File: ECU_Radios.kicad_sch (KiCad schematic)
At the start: 8 parts, among them J19 SMA, J20 SMA

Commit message: addressed PR comments
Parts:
- added C94, C96: 10uF, Capacitor_SMD:C_0603_1608Metric, symbol Device:C_Small
- added J21, J23: SMA, Connector_Coaxial:SMA_Molex_73251-2200_Horizontal, symbol Connector:Conn_Coaxial
- added R117, R119: 100k, Resistor_SMD:R_0603_1608Metric_Pad0.98x0.95mm_HandSolder, symbol Device:R_Small_US
- added U44, U46: ~, UCIRP-KiCAD-Lib:RFM95W, symbol UCIRP-KiCAD-Lib:RFM95W
- renumbered C92 to C93, C93 to C95, J19 to J20, J20 to J22, R113 to R116, R114 to R118, U42 to U43, U43 to U45
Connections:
- net +3.3V: now also C94.1, C96.1, R117.1, R119.1, U44.13 (3.3V), U46.13 (3.3V)
- net GND: now also C94.2, C96.2, J21.2 (Ext), J23.2 (Ext), U44.1 (GND), U44.10 (GND), U44.8 (GND), U46.1 (GND), U46.10 (GND), U46.8 (GND)
- net RADIO_MISO: now also U44.2 (MISO), U46.2 (MISO)
- net RADIO_MOSI: now also U44.3 (MOSI), U46.3 (MOSI)
- net RADIO_SCK: now also U44.4 (SCK), U46.4 (SCK)
- new net: R117.2, U44.5 (~{CS})
- new net: J21.1 (In), U44.9 (ANT)
- new net: R119.2, U46.5 (~{CS})
- new net: J23.1 (In), U46.9 (ANT)
- no-connect marks 8 -> 16
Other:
- note added: "NEED TO ADD DIO, RST, and CS PINS"
- note added: "TRS Radio Module 3"
- note added: "TRS Radio Module 4"
- moved on the sheet: C93, C95, J20, J22, R116, R118, U43, U45

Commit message: Updated schematic with IOC
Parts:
- removed C96: 10uF, Capacitor_SMD:C_0603_1608Metric, symbol Device:C_Small
- removed J23: SMA, Connector_Coaxial:SMA_Molex_73251-2200_Horizontal, symbol Connector:Conn_Coaxial
- removed R119: 100k, Resistor_SMD:R_0603_1608Metric_Pad0.98x0.95mm_HandSolder, symbol Device:R_Small_US
- removed U46: ~, UCIRP-KiCAD-Lib:RFM95W, symbol UCIRP-KiCAD-Lib:RFM95W
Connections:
- net RADIO2_DIO0: now reaches U44.14 (DIO0)
- net RADIO2_DIO1: now reaches U44.15 (DIO1)
- net RADIO2_nCS: now reaches R117.2, U44.5 (~{CS})
- net RADIO2_nRST: now reaches U44.6 (~{RST})
- no-connect marks 16 -> 12
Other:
- note removed: "NEED TO ADD DIO, RST, and CS PINS"
- note removed: "TRS Radio Module 4"
- moved on the sheet: C94, J21, R117, U44

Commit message: Assigned almost all footprints
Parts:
- R116, R117, R118: value 100k -> 100K; footprint Resistor_SMD:R_0603_1608Metric_Pad0.98x0.95mm_HandSolder -> Resistor_SMD:R_0402_1005Metric; Part # Generic 100k 1% 0402 Chip Resistor -> Generic 100K 5% 0402 Resistor
- U43, U44, U45: footprint UCIRP-KiCAD-Lib:RFM95W -> 0UCIRP-KiCAD-Lib:RFM95W
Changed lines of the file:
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@@
 			)
 		)
-		(property "Footprint" "UCIRP-KiCAD-Lib:RFM95W"
+		(property "Footprint" "0UCIRP-KiCAD-Lib:RFM95W"
 			(at 137.16 129.54 0)
 			(effects
@@
 		(on_board yes)
 		(dnp no)
-		(property "Reference" "#PWR0299"
+		(property "Reference" "#PWR0301"
 			(at 172.72 125.73 0)
 			(effects
@@
 			(project "rocket2-ecu"
 				(path "/02606b2c-b376-4ffb-9781-f9cea3f70994/2e42eb37-4c52-4f5f-835d-7e84f50db3a9"
-					(reference "#PWR0299")
+					(reference "#PWR0301")
 					(unit 1)
 				)
@@
 		(on_board yes)
 		(dnp no)
-		(property "Reference" "#PWR0304"
+		(property "Reference" "#PWR0302"
 			(at 191.77 57.15 0)
 			(effects
@@
 			(project "rocket2-ecu"
 				(path "/02606b2c-b376-4ffb-9781-f9cea3f70994/2e42eb37-4c52-4f5f-835d-7e84f50db3a9"
-					(reference "#PWR0304")
+					(reference "#PWR0302")
 					(unit 1)
 				)
@@
 		(on_board yes)
 		(dnp no)
-		(property "Reference" "#PWR0300"
+		(property "Reference" "#PWR0298"
 			(at 158.75 88.9 0)
 			(effects
@@
 			(project "rocket2-ecu"
 				(path "/02606b2c-b376-4ffb-9781-f9cea3f70994/2e42eb37-4c52-4f5f-835d-7e84f50db3a9"
-					(reference "#PWR0300")
+					(reference "#PWR0298")
 					(unit 1)
 				)
@@
 		(on_board yes)
 		(dnp no)
-		(property "Reference" "#PWR0309"
+		(property "Reference" "#PWR0305"
 			(at 227.33 66.04 0)
 			(effects
@@
 			(project "rocket2-ecu"
 				(path "/02606b2c-b376-4ffb-9781-f9cea3f70994/2e42eb37-4c52-4f5f-835d-7e84f50db3a9"
-					(reference "#PWR0309")
+					(reference "#PWR0305")
 					(unit 1)
 				)
@@
 		(on_board yes)
 		(dnp no)
-		(property "Reference" "#PWR0289"
+		(property "Reference" "#PWR0292"
 			(at 104.14 148.59 0)
 			(effects
@@
 			(project "rocket2-ecu"
 				(path "/02606b2c-b376-4ffb-9781-f9cea3f70994/2e42eb37-4c52-4f5f-835d-7e84f50db3a9"
-					(reference "#PWR0289")
+					(reference "#PWR0292")
 					(unit 1)
 				)
@@
 		(on_board yes)
 		(dnp no)
-		(property "Reference" "#PWR0290"
+		(property "Reference" "#PWR0289"
 			(at 59.69 58.42 0)
 			(effects
@@
 			(project "rocket2-ecu"
 				(path "/02606b2c-b376-4ffb-9781-f9cea3f70994/2e42eb37-4c52-4f5f-835d-7e84f50db3a9"
-					(reference "#PWR0290")
+					(reference "#PWR0289")
 					(unit 1)
 				)
@@
 		(on_board yes)
 		(dnp no)
-		(property "Reference" "#PWR0292"
+		(property "Reference" "#PWR0290"
 			(at 91.44 57.15 0)
 			(effects
@@
 			(project "rocket2-ecu"
 				(path "/02606b2c-b376-4ffb-9781-f9cea3f70994/2e42eb37-4c52-4f5f-835d-7e84f50db3a9"
-					(reference "#PWR0292")
+					(reference "#PWR0290")
 					(unit 1)
 				)
@@
 			)
 		)
-		(property "Footprint" "UCIRP-KiCAD-Lib:RFM95W"
+		(property "Footprint" "0UCIRP-KiCAD-Lib:RFM95W"
 			(at 91.44 69.85 0)
 			(effects
@@
 			)
 		)
-		(property "Value" "100k"
+		(property "Value" "100K"
 			(at 62.23 58.42 0)
 			(effects
@@
 			)
 		)
-		(property "Footprint" "Resistor_SMD:R_0603_1608Metric_Pad0.98x0.95mm_HandSolder"
+		(property "Footprint" "Resistor_SMD:R_0402_1005Metric"
 			(at 59.69 57.15 0)
 			(effects
@@
 			)
 		)
-		(property "Part #" "Generic 100k 1% 0402 Chip Resistor"
+		(property "Part #" "Generic 100K 5% 0402 Resistor"
 			(at 59.69 57.15 0)
 			(effects
@@
 		(on_board yes)
 		(dnp no)
-		(property "Reference" "#PWR0302"
+		(property "Reference" "#PWR0299"
 			(at 160.02 58.42 0)
 			(effects
@@
 			(project "rocket2-ecu"
 				(path "/02606b2c-b376-4ffb-9781-f9cea3f70994/2e42eb37-4c52-4f5f-835d-7e84f50db3a9"
-					(reference "#PWR0302")
+					(reference "#PWR0299")
 					(unit 1)
 				)
@@
 		(on_board yes)
 		(dnp no)
-		(property "Reference" "#PWR0296"
+		(property "Reference" "#PWR0294"
 			(at 127 58.42 0)
 			(effects
@@
 			(project "rocket2-ecu"
 				(path "/02606b2c-b376-4ffb-9781-f9cea3f70994/2e42eb37-4c52-4f5f-835d-7e84f50db3a9"
-					(reference "#PWR0296")
+					(reference "#PWR0294")
 					(unit 1)
 				)
@@
 		(on_board yes)
 		(dnp no)
-		(property "Reference" "#PWR0305"
+		(property "Reference" "#PWR0303"
 			(at 191.77 95.25 0)
 			(effects
@@
 			(project "rocket2-ecu"
 				(path "/02606b2c-b376-4ffb-9781-f9cea3f70994/2e42eb37-4c52-4f5f-835d-7e84f50db3a9"
-					(reference "#PWR0305")
+					(reference "#PWR0303")
 					(unit 1)
 				)
@@
 		(on_board yes)
 		(dnp no)
-		(property "Reference" "#PWR0297"
+		(property "Reference" "#PWR0295"
 			(at 127 66.04 0)
 			(effects
@@
 			(project "rocket2-ecu"
 				(path "/02606b2c-b376-4ffb-9781-f9cea3f70994/2e42eb37-4c52-4f5f-835d-7e84f50db3a9"
-					(reference "#PWR0297")
+					(reference "#PWR0295")
 					(unit 1)
 				)
@@
 		(on_board yes)
 		(dnp no)
-		(property "Reference" "#PWR0298"
+		(property "Reference" "#PWR0300"
 			(at 172.72 118.11 0)
 			(effects
@@
 			(project "rocket2-ecu"
 				(path "/02606b2c-b376-4ffb-9781-f9cea3f70994/2e42eb37-4c52-4f5f-835d-7e84f50db3a9"
-					(reference "#PWR0298")
+					(reference "#PWR0300")
 					(unit 1)
 				)
@@
 		(on_board yes)
 		(dnp no)
-		(property "Reference" "#PWR0291"
+		(property "Reference" "#PWR0293"
 			(at 105.41 118.11 0)
 			(effects
@@
 			(project "rocket2-ecu"
 				(path "/02606b2c-b376-4ffb-9781-f9cea3f70994/2e42eb37-4c52-4f5f-835d-7e84f50db3a9"
-					(reference "#PWR0291")
+					(reference "#PWR0293")
 					(unit 1)
 				)
@@
 			)
 		)
-		(property "Value" "100k"
+		(property "Value" "100K"
 			(at 162.56 58.42 0)
 			(effects
@@
 			)
 		)
-		(property "Footprint" "Resistor_SMD:R_0603_1608Metric_Pad0.98x0.95mm_HandSolder"
+		(property "Footprint" "Resistor_SMD:R_0402_1005Metric"
 			(at 160.02 57.15 0)
 			(effects
@@
 			)
 		)
-		(property "Part #" "Generic 100k 1% 0402 Chip Resistor"
+		(property "Part #" "Generic 100K 5% 0402 Resistor"
 			(at 160.02 57.15 0)
 			(effects
@@
 		(on_board yes)
 		(dnp no)
-		(property "Reference" "#PWR0295"
+		(property "Reference" "#PWR0297"
 			(at 137.16 154.94 0)
 			(effects
@@
 			(project "rocket2-ecu"
 				(path "/02606b2c-b376-4ffb-9781-f9cea3f70994/2e42eb37-4c52-4f5f-835d-7e84f50db3a9"
-					(reference "#PWR0295")
+					(reference "#PWR0297")
 					(unit 1)
 				)
@@
 			)
 		)
-		(property "Footprint" "UCIRP-KiCAD-Lib:RFM95W"
+		(property "Footprint" "0UCIRP-KiCAD-Lib:RFM95W"
 			(at 191.77 69.85 0)
 			(effects
@@
 		(on_board yes)
 		(dnp no)
-		(property "Reference" "#PWR0293"
+		(property "Reference" "#PWR0291"
 			(at 91.44 95.25 0)
 			(effects
@@
 			(project "rocket2-ecu"
 				(path "/02606b2c-b376-4ffb-9781-f9cea3f70994/2e42eb37-4c52-4f5f-835d-7e84f50db3a9"
-					(reference "#PWR0293")
+					(reference "#PWR0291")
 					(unit 1)
 				)
@@
 			)
 		)
-		(property "Value" "100k"
+		(property "Value" "100K"
 			(at 107.95 118.11 0)
 			(effects
@@
 			)
 		)
-		(property "Footprint" "Resistor_SMD:R_0603_1608Metric_Pad0.98x0.95mm_HandSolder"
+		(property "Footprint" "Resistor_SMD:R_0402_1005Metric"
 			(at 105.41 116.84 0)
 			(effects
@@
 			)
 		)
-		(property "Part #" "Generic 100k 1% 0402 Chip Resistor"
+		(property "Part #" "Generic 100K 5% 0402 Resistor"
 			(at 105.41 116.84 0)
 			(effects
@@
 		(on_board yes)
 		(dnp no)
-		(property "Reference" "#PWR0294"
+		(property "Reference" "#PWR0296"
 			(at 137.16 116.84 0)
 			(effects
@@
 			(project "rocket2-ecu"
 				(path "/02606b2c-b376-4ffb-9781-f9cea3f70994/2e42eb37-4c52-4f5f-835d-7e84f50db3a9"
-					(reference "#PWR0294")
+					(reference "#PWR0296")
 					(unit 1)
 				)
@@
 		(on_board yes)
 		(dnp no)
-		(property "Reference" "#PWR0308"
+		(property "Reference" "#PWR0304"
 			(at 227.33 58.42 0)
 			(effects
@@
 			(project "rocket2-ecu"
 				(path "/02606b2c-b376-4ffb-9781-f9cea3f70994/2e42eb37-4c52-4f5f-835d-7e84f50db3a9"
-					(reference "#PWR0308")
-					(unit 1)
-				)
+					(reference "#PWR0304")
+					(unit 1)
+				)

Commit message: new BOM
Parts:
- C93, C94, C95: Part # Generic 0603 10uF 6.3V X7R MLCC -> Generic CAP CER 10UF 50V X7R 0603
- J20, J21, J22: Part # 732512200 -> 0732512200
- R116, R117, R118: Part # Generic 100K 5% 0402 Resistor -> Generic RES SMD 100K OHM 1% 1/16W 0402
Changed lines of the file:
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@@
 			)
 		)
-		(property "Datasheet" " ~"
+		(property "Datasheet" "https://www.molex.com/en-us/products/part-detail/732512200?display=pdf"
 			(at 158.75 77.47 0)
 			(effects
@@
 			)
 		)
-		(property "Part #" "732512200"
+		(property "Part #" "0732512200"
 			(at 158.75 77.47 0)
 			(effects
@@
 			)
 		)
-		(property "Datasheet" " ~"
+		(property "Datasheet" "https://www.molex.com/en-us/products/part-detail/732512200?display=pdf"
 			(at 104.14 137.16 0)
 			(effects
@@
 			)
 		)
-		(property "Part #" "732512200"
+		(property "Part #" "0732512200"
 			(at 104.14 137.16 0)
 			(effects
@@
 			)
 		)
-		(property "Part #" "Generic 100K 5% 0402 Resistor"
+		(property "Part #" "Generic RES SMD 100K OHM 1% 1/16W 0402"
 			(at 59.69 57.15 0)
 			(effects
@@
 			)
 		)
-		(property "Part #" "Generic 0603 10uF 6.3V X7R MLCC"
+		(property "Part #" "Generic CAP CER 10UF 50V X7R 0603"
 			(at 127 57.15 0)
 			(effects
@@
 			)
 		)
-		(property "Part #" "Generic 0603 10uF 6.3V X7R MLCC"
+		(property "Part #" "Generic CAP CER 10UF 50V X7R 0603"
 			(at 172.72 116.84 0)
 			(effects
@@
 			)
 		)
-		(property "Datasheet" " ~"
+		(property "Datasheet" "https://www.molex.com/en-us/products/part-detail/732512200?display=pdf"
 			(at 58.42 77.47 0)
 			(effects
@@
 			)
 		)
-		(property "Part #" "732512200"
+		(property "Part #" "0732512200"
 			(at 58.42 77.47 0)
 			(effects
@@
 			)
 		)
-		(property "Part #" "Generic 100K 5% 0402 Resistor"
+		(property "Part #" "Generic RES SMD 100K OHM 1% 1/16W 0402"
 			(at 160.02 57.15 0)
 			(effects
@@
 			)
 		)
-		(property "Part #" "Generic 100K 5% 0402 Resistor"
+		(property "Part #" "Generic RES SMD 100K OHM 1% 1/16W 0402"
 			(at 105.41 116.84 0)
 			(effects
@@
 			)
 		)
-		(property "Part #" "Generic 0603 10uF 6.3V X7R MLCC"
+		(property "Part #" "Generic CAP CER 10UF 50V X7R 0603"
 			(at 227.33 57.15 0)
 			(effects

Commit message: Finished
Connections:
- net RADIO1_DIO0: no longer names the net of U45.14 (DIO0)
- no-connect marks 12 -> 13
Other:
- note added: "Removed DIO0 so we have vsense"
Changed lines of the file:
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@@
+	)
+	(no_connect
+		(at 207.01 62.23)
 	)
 	(no_connect
@@
 		)
 	)
+	(text "Removed DIO0 so we have vsense"
+		(exclude_from_sim no)
+		(at 249.682 61.976 0)
+		(effects
+			(font
+				(size 1.27 1.27)
+				(color 255 40 86 1)
+			)
+		)
+	)
 	(text "TRS Radio Module 3\n"
 		(exclude_from_sim no)
@@
 				(hide yes)
 			)
-		)
-	)
-	(global_label "RADIO1_DIO0"
-		(shape input)
-		(at 207.01 62.23 0)
-		(fields_autoplaced yes)
-		(effects
-			(font
-				(size 1.27 1.27)
-			)
-			(justify left)
-		)
-		(property "Intersheetrefs" "${INTERSHEET_REFS}"
-			(at 222.151 62.23 0)
-			(effects
-				(font
-					(size 1.27 1.27)
-				)
-				(justify left)
-				(hide yes)
-			)

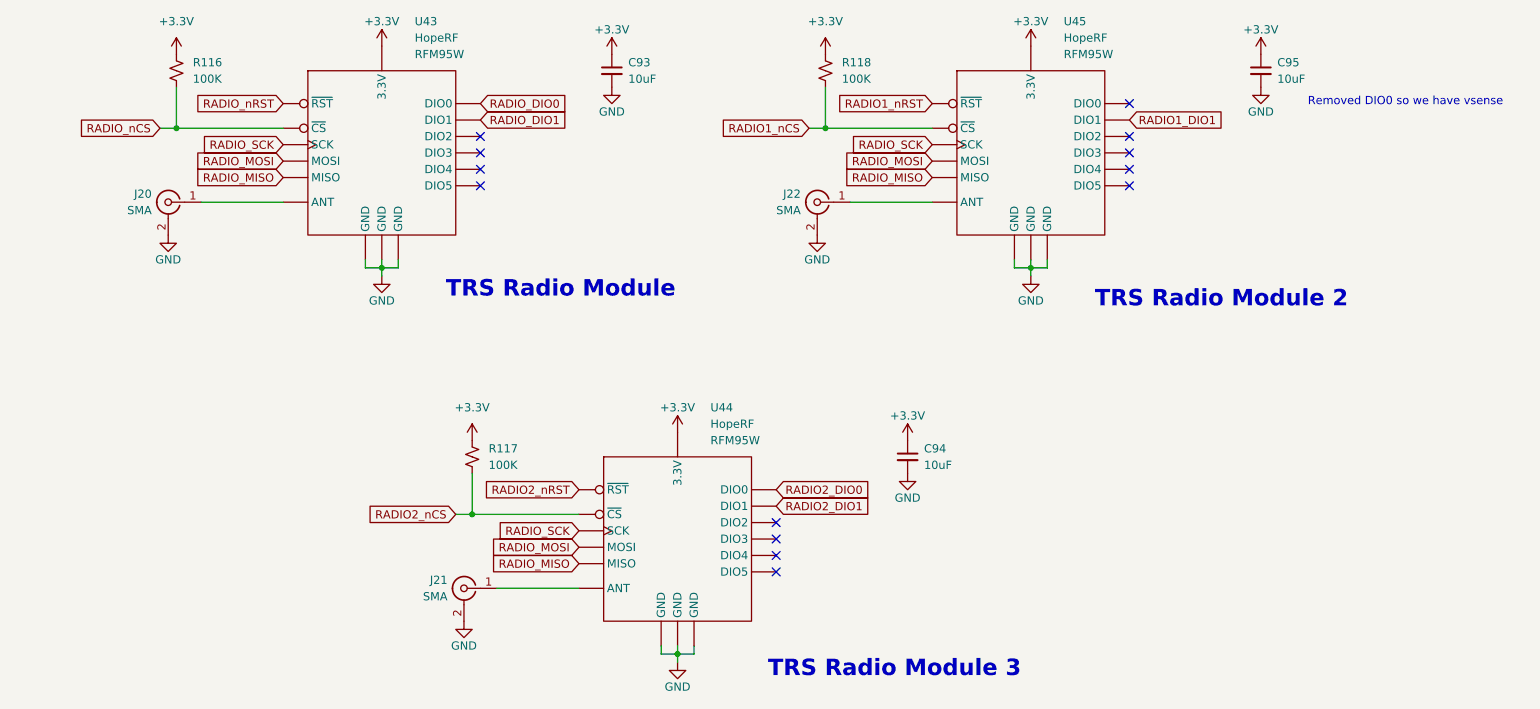
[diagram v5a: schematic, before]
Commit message: REDS updated with diodes and hierarchy to main micro
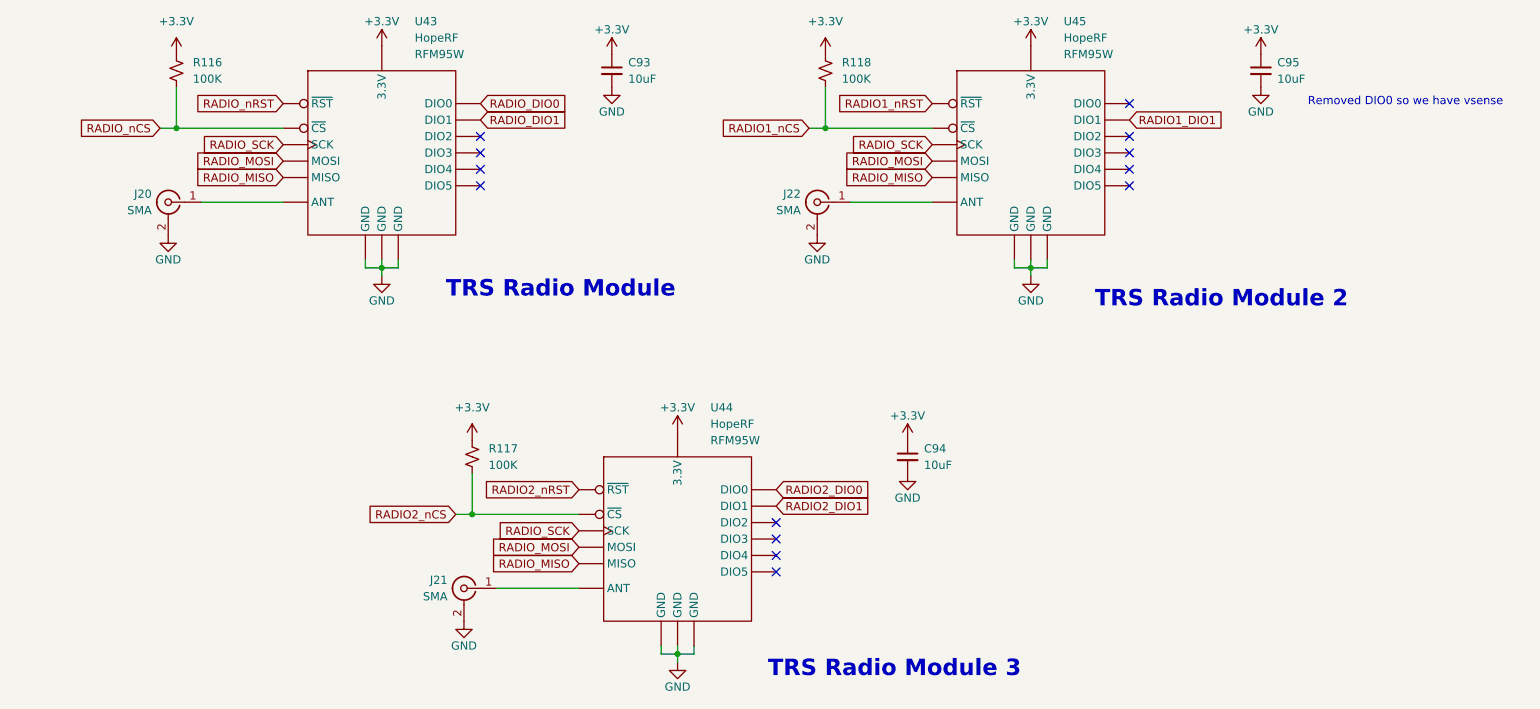
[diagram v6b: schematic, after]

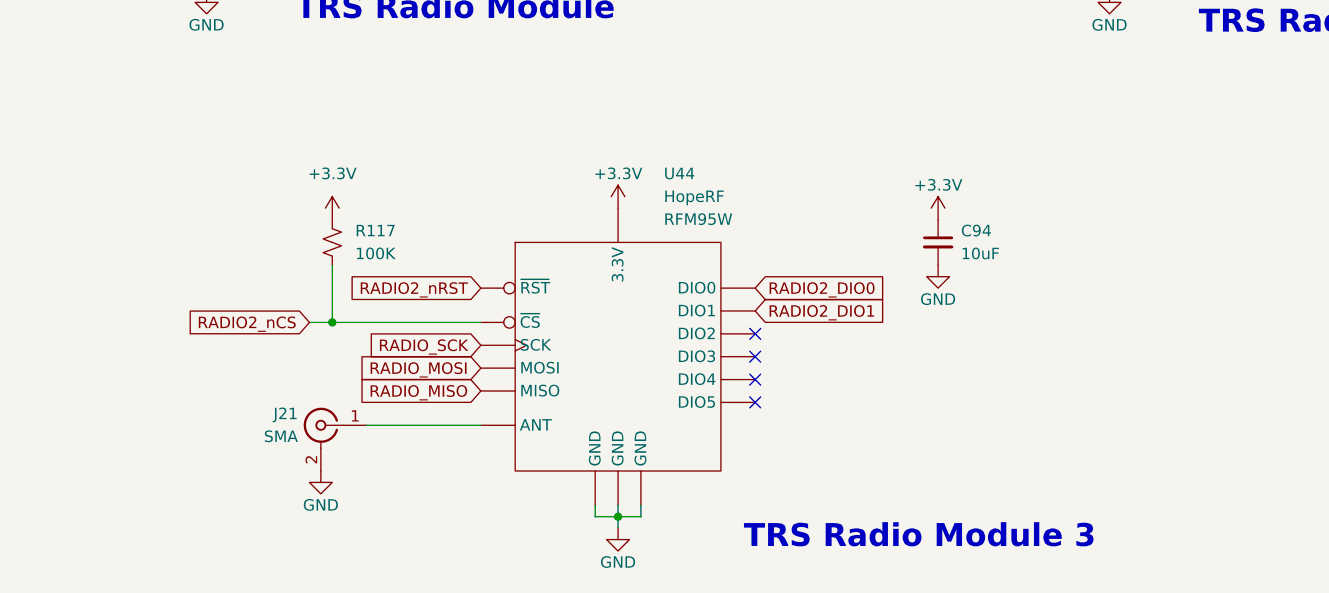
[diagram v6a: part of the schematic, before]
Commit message: 3/4 DC-DC converters done
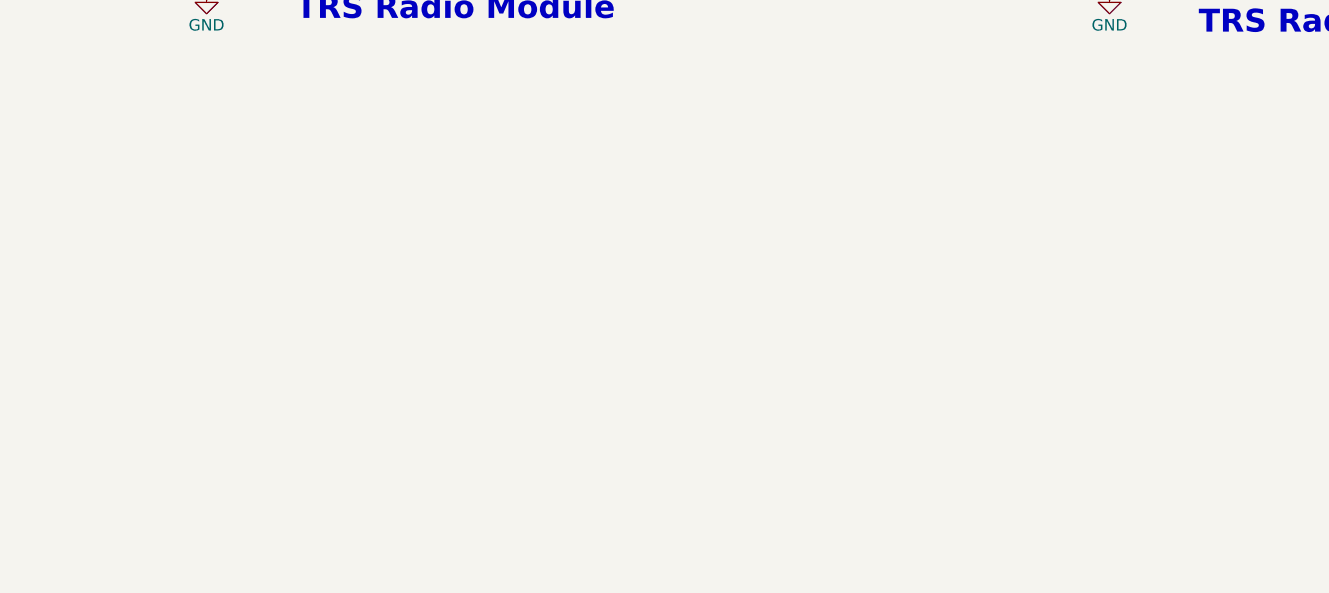
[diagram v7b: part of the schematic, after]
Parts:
- removed C94: 10uF, Capacitor_SMD:C_0603_1608Metric, symbol Device:C_Small
- removed J21: SMA, Connector_Coaxial:SMA_Molex_73251-2200_Horizontal, symbol Connector:Conn_Coaxial
- removed R117: 100K, Resistor_SMD:R_0402_1005Metric, symbol Device:R_Small_US
- removed U44: ~, 0UCIRP-KiCAD-Lib:RFM95W, symbol UCIRP-KiCAD-Lib:RFM95W
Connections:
- no-connect marks 13 -> 9
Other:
- note removed: "TRS Radio Module 3"

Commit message: ALMOST
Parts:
- added D11, D39: LED, LED_SMD:LED_0603_1608Metric_Pad1.05x0.95mm_HandSolder, symbol Device:LED_Small
- added R13, R9: 100, Resistor_SMD:R_0402_1005Metric, symbol Device:R_Small_US
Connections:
- net GND: now also D11.1 (K), D39.1 (K)
- new net: D39.2 (A), R13.1
- new net: D11.2 (A), R9.1
- new net RADIO0_LED: R9.2
- new net RADIO1_LED: R13.2
